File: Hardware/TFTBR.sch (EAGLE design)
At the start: 6 parts, among them IC1 74HC2G125, J1 SPI-LCD

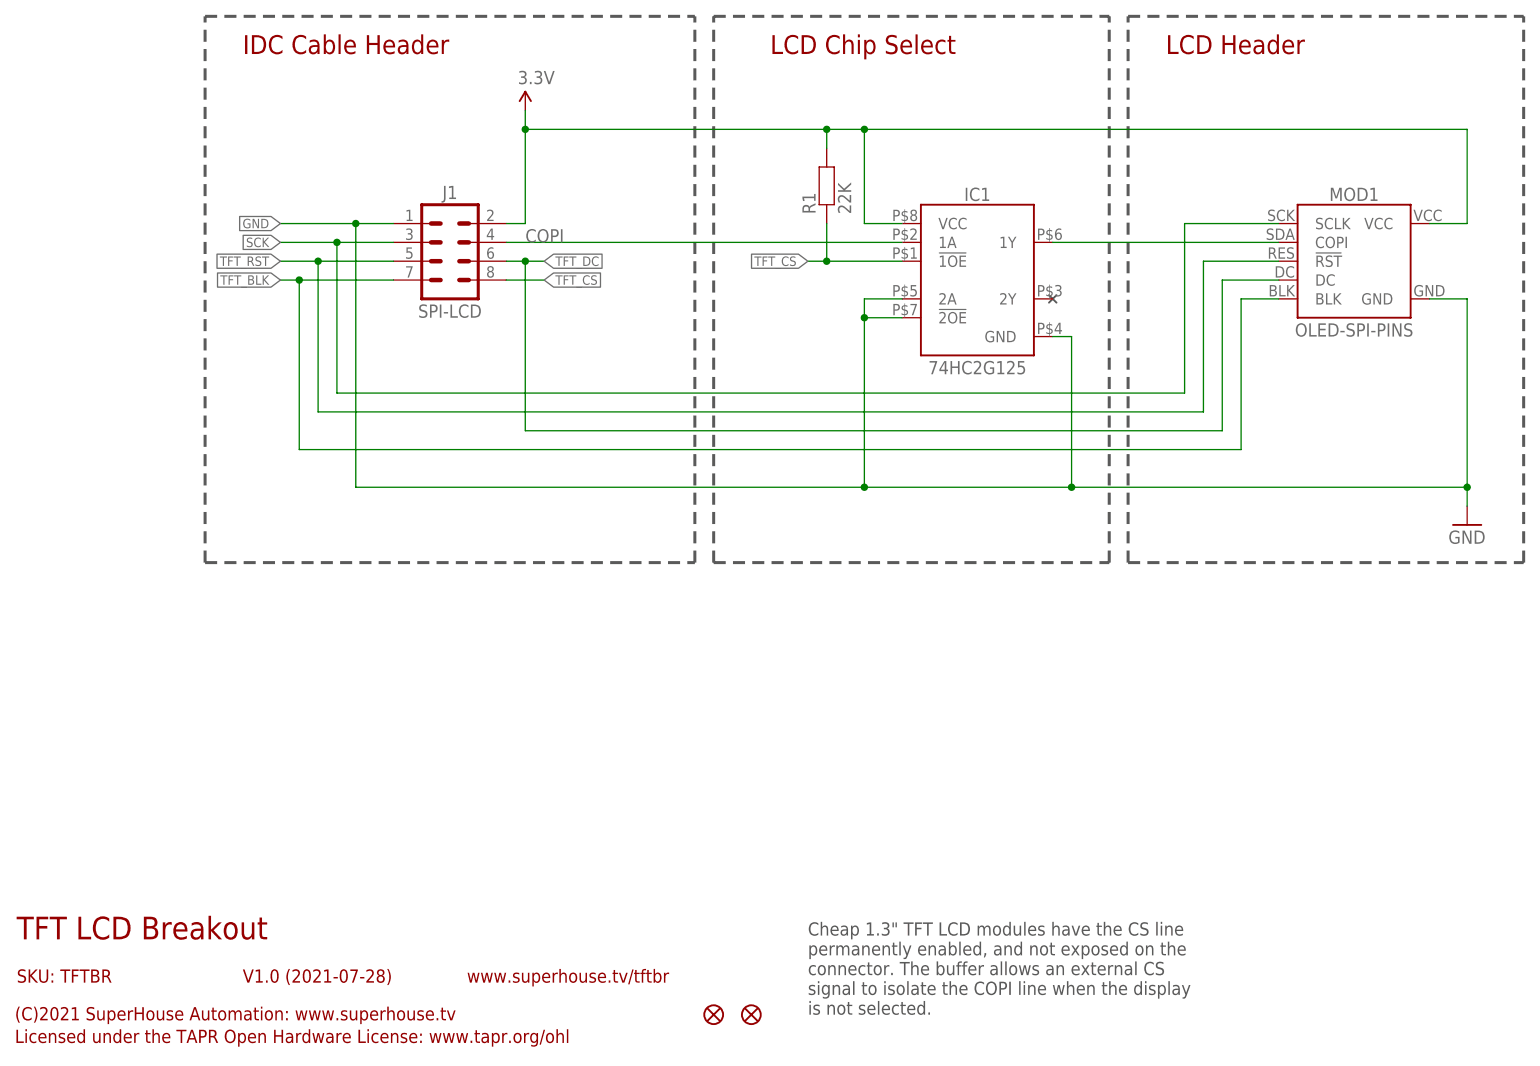
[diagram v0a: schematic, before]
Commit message: Changed to 1.54 inch display.
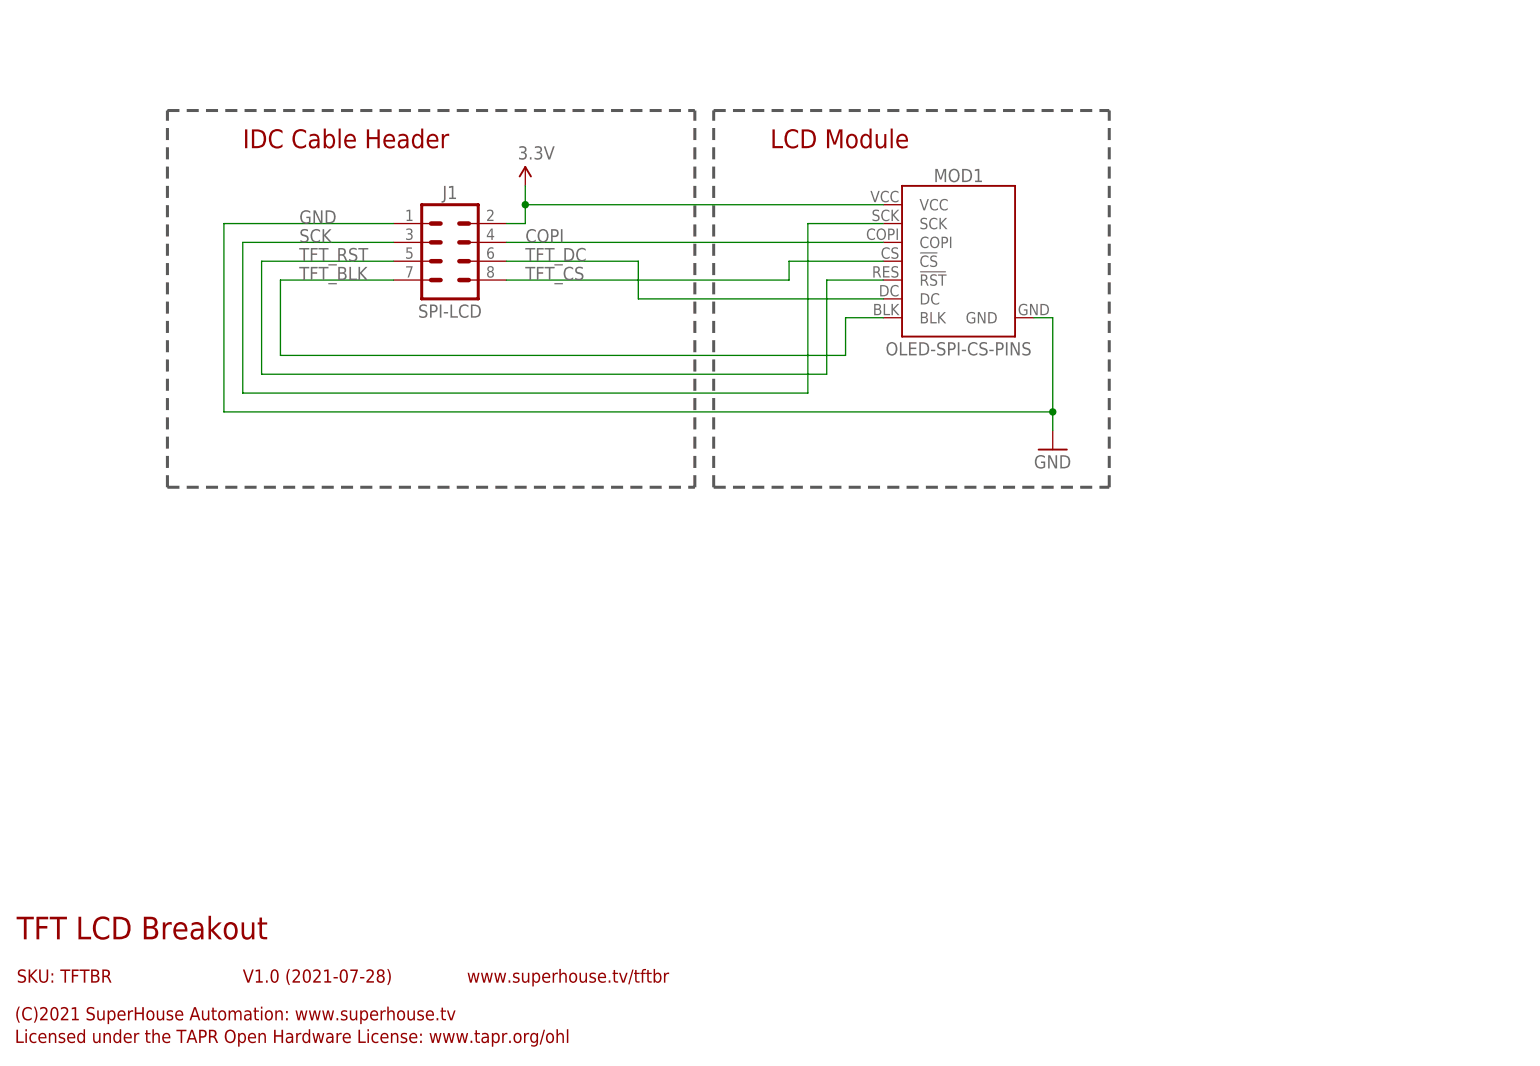
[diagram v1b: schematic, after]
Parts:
- removed FID1, FID2: FIDUCIAL1X2.5, SuperHouse-Symbols:FIDUCIAL1X2.5
- removed IC1: 74HC2G125, SuperHouse-ICs:74HC2G125-TSSOP8
- removed R1: 22K, SuperHouse-Resistors:RESISTOR0603
- MOD1: value OLED-SPI-PINS -> OLED-SPI-CS-PINS; device SuperHouse-Displays:OLED-SPI-PINS -> SuperHouse-Displays:OLED-SPI-CS-PINS
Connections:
- removed net N$1: IC1.1Y, MOD1.COPI
- net 3.3V: no longer IC1.VCC, R1.2
- net COPI: now also MOD1.COPI; no longer IC1.1A
- net GND: no longer IC1.!2OE, IC1.2A, IC1.GND
- net SCK: now also MOD1.SCK; no longer MOD1.SCLK
- net TFT_CS: now also MOD1.!CS; no longer IC1.!1OE, R1.1
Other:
- note added: "LCD Module"
- note removed: "Cheap 1.3" TFT LCD modules have the CS line permanently enabled, and not exposed on the connector. The buffer allows an external CS signal to isolate the COPI line when the display is not selected."
- note removed: "LCD Chip Select"
- note removed: "LCD Header"
